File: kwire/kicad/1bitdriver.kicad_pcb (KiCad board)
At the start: 2 copper layers, 86.4 x 44.5 mm, 50 parts, among them J101 CONN_01X02, Q401 PMOS, Q402 NMOS, Q403 NMOS, Q404 PMOS, Q501 PMOS, Q502 NMOS, Q503 NMOS, Q504 PMOS, Q601 PMOS, Q602 NMOS, Q603 NMOS, Q604 PMOS, Q701 PMOS, Q702 NMOS, Q703 PMOS, Q704 NMOS, Q705 PMOS, Q706 NMOS, Q801 PMOS, Q802 NMOS, Q803 PMOS, Q804 NMOS, Q805 PMOS, Q806 NMOS, Q901 PMOS, Q902 NMOS, Q903 PMOS, Q904 NMOS, Q905 PMOS, Q906 NMOS

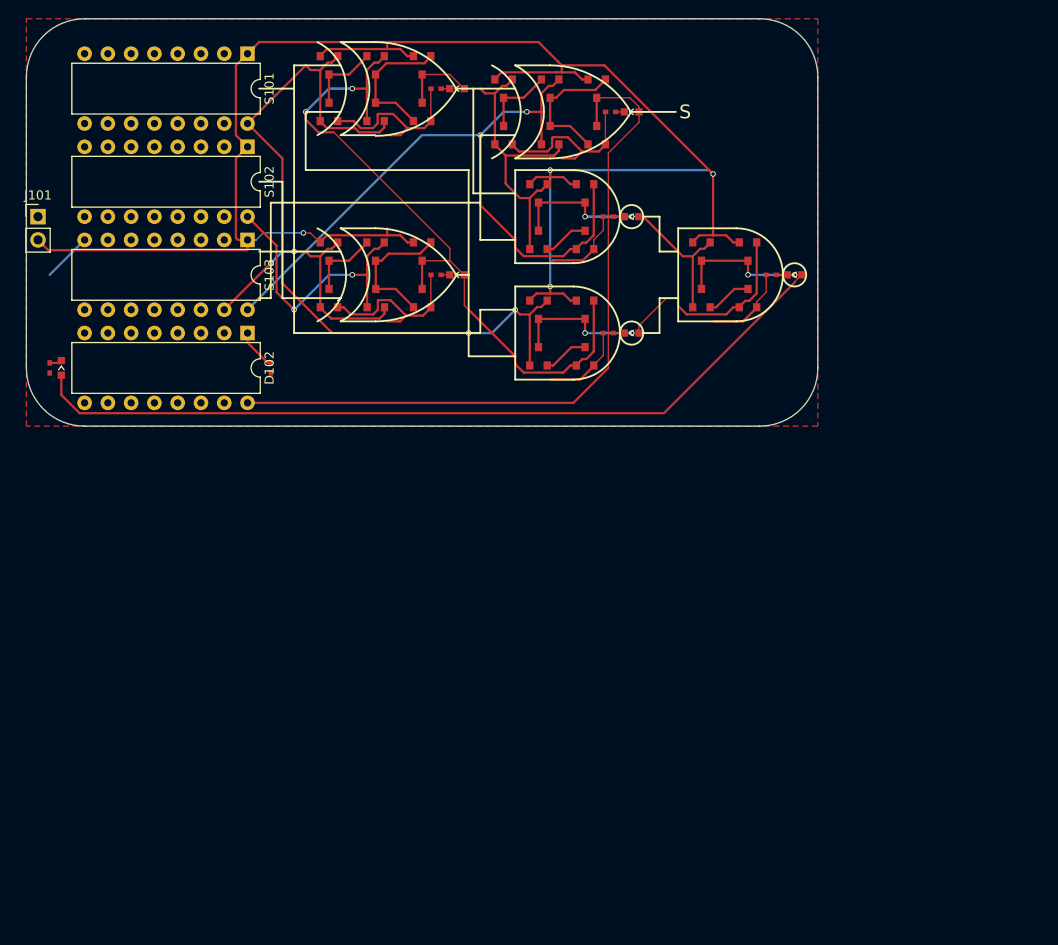
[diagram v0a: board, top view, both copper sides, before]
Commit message: Now parses multiple files
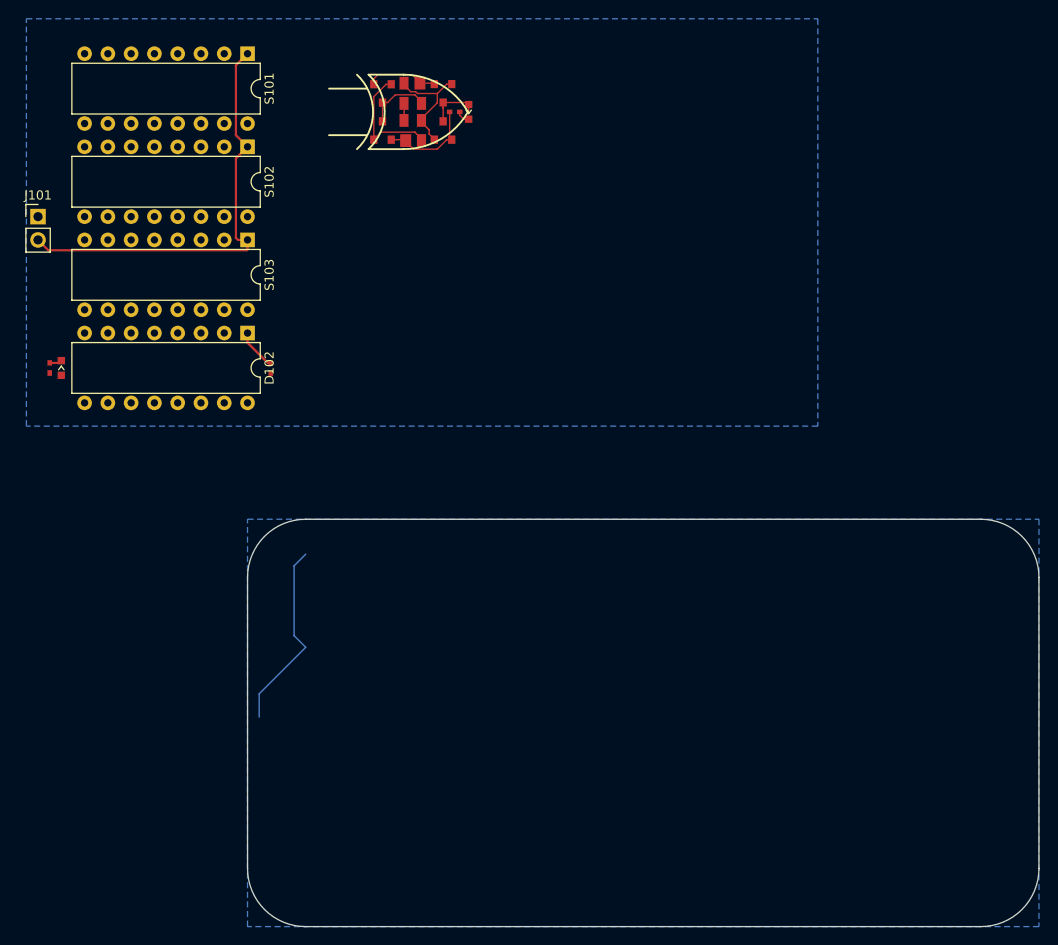
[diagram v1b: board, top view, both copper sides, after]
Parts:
- removed D401, D501, D601, D801, D901: LED_Small, KwanSystems:D_0603
- removed Q401, Q404, Q501, Q504, Q601, Q604, Q703, Q801, Q803, Q805, Q901, Q903, Q905: PMOS, KwanSystems:SOT-23
- removed Q402, Q403, Q502, Q503, Q602, Q603, Q704, Q802, Q804, Q806, Q902, Q904, Q906: NMOS, KwanSystems:SOT-23
- removed R401, R501, R601, R801, R901: RESISTOR, KwanSystems:SMD_0402
- added Q203: PMOS_BODY, KwanSystems:SOT-143, F.Cu at (112.0, 52.6)
- added Q204: NMOS_BODY, KwanSystems:SOT-143, F.Cu at (112.0, 56.6)
- D201: renamed from D701; value LED_Small -> Y
- moved Q201 6.60 mm to (108.7, 52.6)
- moved Q202 6.19 mm to (108.7, 56.6)
- moved Q205 3.81 mm to (115.3, 52.6)
- moved R201 3.25 mm to (116.6, 54.6)
- moved Q206 3.06 mm to (115.3, 56.6)
- moved D201 2.84 mm to (118.1, 54.6), turned to 90 degrees
- renumbered Q701 to Q201, Q702 to Q202, Q705 to Q205, Q706 to Q206, R701 to R201
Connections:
- net /bit0/adder/AxorB renamed /bit0/Y
- net Net-(D701-Pad1) renamed /bit0/Y-
- net Net-(Q701-Pad3) renamed /bit0/#A
- net Net-(Q703-Pad3) renamed /bit0/#Y
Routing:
- net VCC: track 204.3 -> 55.3 mm, vias 4 -> 0
- net /K: track 105.7 -> 0.00 mm, vias 2 -> 0
- net /S: track 78.9 -> 0.00 mm
- net /C: track 78.5 -> 0.00 mm, vias 2 -> 0
- net /bit0/adder/B: track 75.5 -> 0.00 mm, vias 2 -> 0
- net /A: track 85.0 -> 13.2 mm, vias 2 -> 0
- net GND: track 89.8 -> 31.6 mm
- net /bit0/adder/#AandB: track 38.2 -> 0.00 mm, vias 2 -> 0
- net /bit0/Y: track 42.9 -> 5.75 mm
- net /bit0/adder/#AxorBandC: track 31.8 -> 0.00 mm, vias 2 -> 0
- net /SUB: track 29.9 -> 0.00 mm, vias 2 -> 0
- net /B: track 29.9 -> 2.10 mm, vias 2 -> 0
- net Net-(Q803-Pad3): track 15.0 -> 0.00 mm
- net Net-(Q903-Pad3): track 14.9 -> 0.00 mm
- net Net-(Q901-Pad3): track 8.07 -> 0.00 mm
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- added copper zone on B.Cu, net GND
- removed copper zone on F.Cu, net GND
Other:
- board size 86.4 x 44.5 mm -> 86.4 x 44.4 mm
- board text removed: "S"
